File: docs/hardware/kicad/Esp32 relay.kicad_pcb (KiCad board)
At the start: 2 copper layers, 137.5 x 86 mm, 149 parts, among them J1 Conn_01x05_Pin, J10 Screw_Terminal_01x04, J11 Screw_Terminal_01x05, J12 Screw_Terminal_01x04, J13 Screw_Terminal_01x05, J14 GPIO, J15 SPI, J2 Conn_01x05_Pin, J3 Screw_Terminal_01x02, J4 USB_C_Receptacle_USB2.0_16P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

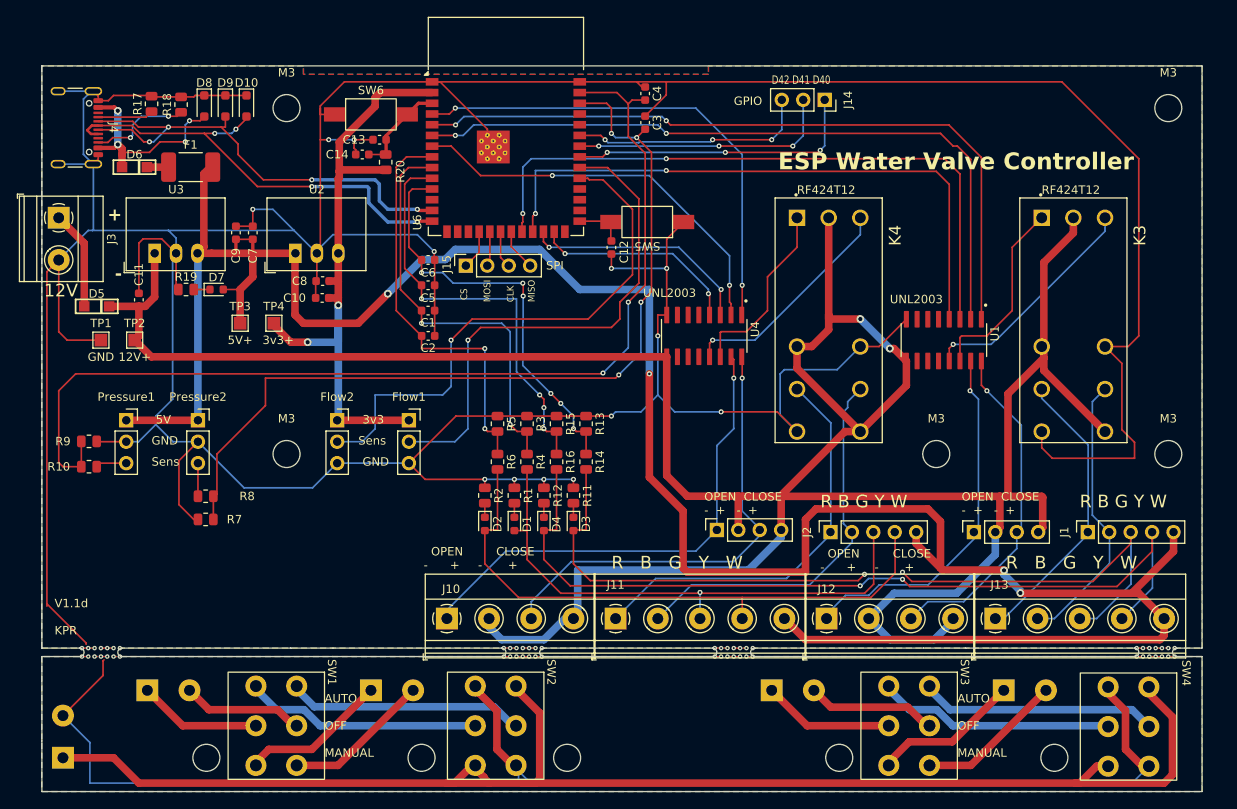
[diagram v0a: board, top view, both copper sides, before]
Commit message: Updates PCB design to 1.2a
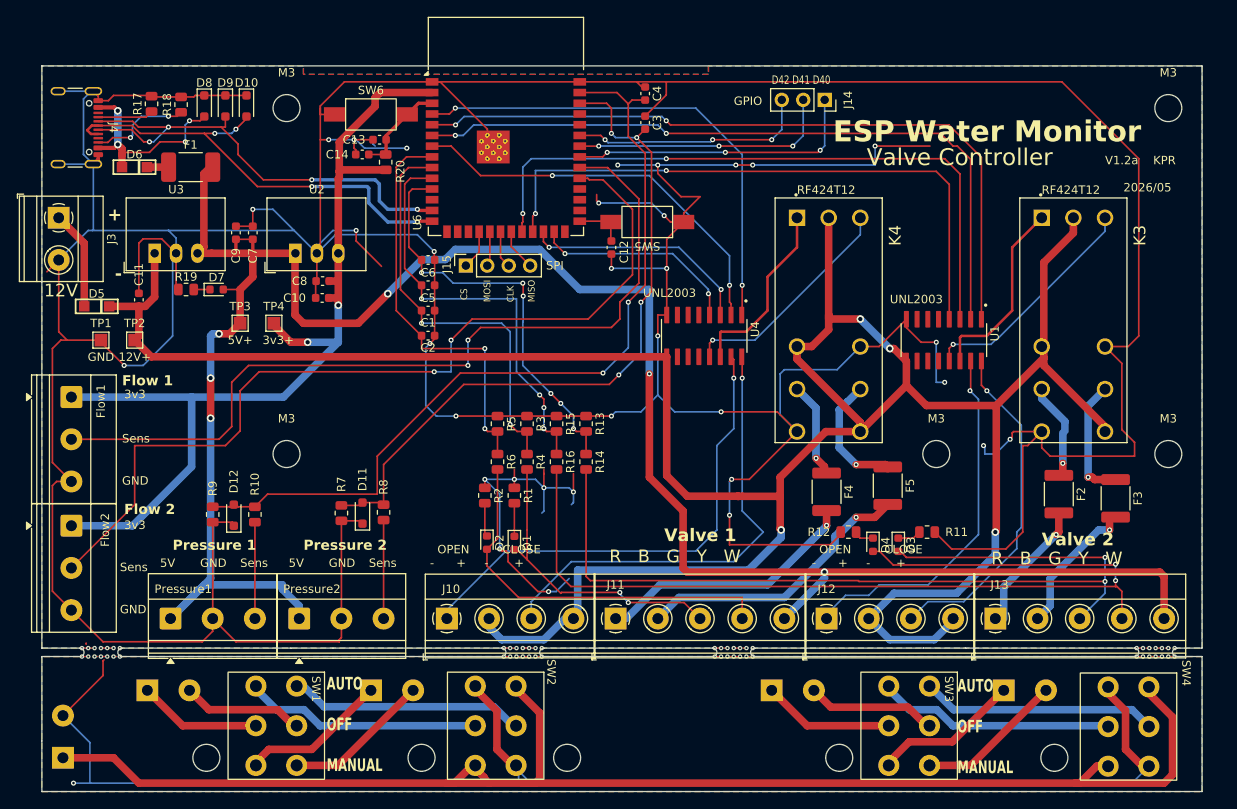
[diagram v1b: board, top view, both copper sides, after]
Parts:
- removed J1, J2: Conn_01x05_Pin, Connector_PinSocket_2.54mm:PinSocket_1x05_P2.54mm_Vertical
- removed Led1, Led2: Conn_01x04_Socket, Connector_PinSocket_2.54mm:PinSocket_1x04_P2.54mm_Vertical
- added D11: D_TVS, Diode_SMD:D_SOD-323_HandSoldering, F.Cu at (88.5, 98.0)
- added D12: D_TVS, Diode_SMD:D_SOD-323_HandSoldering, F.Cu at (73.2, 98.2)
- added F2: 1.5A, Fuse:Fuse_1812_4532Metric_Pad1.30x3.40mm_HandSolder, F.Cu at (171.0, 95.8)
- added F3: 1.5A, Fuse:Fuse_1812_4532Metric_Pad1.30x3.40mm_HandSolder, F.Cu at (177.8, 96.2)
- added F4: 1.5A, Fuse:Fuse_1812_4532Metric_Pad1.30x3.40mm_HandSolder, F.Cu at (143.5, 95.5)
- added F5: 1.5A, Fuse:Fuse_1812_4532Metric_Pad1.30x3.40mm_HandSolder, F.Cu at (150.8, 94.8)
- Flow1, Flow2, Pressure1, Pressure2: value Conn_01x03_Pin -> Screw_Terminal_01x03; footprint Connector_PinSocket_2.54mm:PinSocket_1x03_P2.54mm_Vertical -> TerminalBlock_Phoenix:TerminalBlock_Phoenix_MKDS-1,5-3_1x03_P5.00mm_Horizontal
- R1, R11, R19: value 400R -> 1K
- R12, R2: value 400R -> 1.8K
- moved R11 42.1 mm to (155.4, 100.2), turned to 180 degrees
- moved Flow1 40.1 mm to (54.0, 84.2), turned to -90 degrees
- moved D4 39.1 mm to (149.0, 101.8)
- moved D3 38.6 mm to (152.0, 101.8)
- moved R12 36.3 mm to (146.1, 100.2), turned to 0 degrees
- moved Flow2 33.9 mm to (54.0, 99.5), turned to -90 degrees
- moved Pressure2 26.4 mm to (81.0, 110.5)
- moved Pressure1 24.1 mm to (65.8, 110.5)
- moved R8 21.2 mm to (91.0, 97.9), turned to -90 degrees
- moved R10 20.5 mm to (75.8, 98.2), turned to -90 degrees
- moved R9 17.0 mm to (70.8, 98.2), turned to 90 degrees
- moved R7 16.1 mm to (86.0, 98.0), turned to 90 degrees
- moved D1 2.25 mm to (106.5, 101.5)
- moved D2 2.23 mm to (103.2, 101.5)
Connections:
- J13 pad 1: Net-(J1-Pin_1) -> Net-(J13-Pin_1)
- J13 pad 2: Net-(J1-Pin_2) -> Net-(J13-Pin_2)
- K3 pad 11: Net-(J1-Pin_1) -> Net-(F2-Pad1)
- K3 pad 21: Net-(J1-Pin_2) -> Net-(F3-Pad1)
- K4 pad 11: Net-(J11-Pin_1) -> Net-(F4-Pad1)
- K4 pad 21: Net-(J11-Pin_2) -> Net-(F5-Pad1)
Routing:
- net Earth: track 777.0 -> 967.9 mm, vias 13 -> 34
- net /GPIO38: track 64.3 -> 105.5 mm, vias 1 -> 2
- net /3v3: track 74.4 -> 114.0 mm
- net /GPIO39: track 60.9 -> 99.4 mm, vias 1 -> 2
- net /5V: track 298.7 -> 263.7 mm, vias 4 -> 6
- net Net-(J1-Pin_1): track 34.6 -> 0.00 mm
- net Net-(J1-Pin_2): track 33.4 -> 0.00 mm
- net Net-(D1-A): track 64.7 -> 36.0 mm, vias 1 -> 2
- net +12V: track 518.6 -> 492.5 mm, vias 2 -> 4
- net Net-(D2-A): track 71.5 -> 46.2 mm
- net /GPIO1: track 123.3 -> 99.4 mm
- net /GPIO2: track 103.5 -> 84.3 mm
- net Net-(J11-Pin_1): track 48.5 -> 31.4 mm, vias 0 -> 1
- net Net-(J13-Pin_2): track 0.00 -> 16.6 mm, vias 0 -> 1
- net Net-(J13-Pin_1): track 0.00 -> 16.2 mm, vias 0 -> 1
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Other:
- board text added: "ESP Water Monitor"
- board text added: "Flow 1"
- board text added: "Flow 2"
- board text added: "Pressure 1"
- board text added: "Pressure 2"
- board text added: "TOGGLE SWITCH BOARD V1.2"
- board text added: "V1.2a KPR 2026/05"
- board text added: "Valve 1"
- board text added: "Valve 2"
- board text added: "Valve Controller"
- board text removed: "ESP Water Valve Controller"
- board text removed: "TOGGLE SWITCH BOARD V1.1"
- board text removed: "V1.1d KPR"
